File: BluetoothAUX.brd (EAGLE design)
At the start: 19.7 x 27.9 mm, 15 parts, among them IC2 TPA6132A2, J3 AUDIO_JACK_TRRSSMD_RA, J4 USB

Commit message: Make smaller
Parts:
- removed JP10: PROG, pinhead:1X08
- added JP1: PROG, pinhead:1X07
- moved R2 17.3 mm to (91.1, 24.4), turned to 90 degrees
- moved RN1 17.2 mm to (86.8, 24.4)
- moved R3 7.63 mm to (89.2, 24.4)
- moved LED1 4.44 mm to (79.4, 24.4)
- moved RN2 4.29 mm to (84.0, 24.4)
- moved IC2 3.52 mm to (79.7, 33.2)
- moved J3 3.49 mm to (87.6, 45.7)
- moved J4 3.35 mm to (78.7, 44.3)
- moved C5 3.33 mm to (81.6, 38.9)
- moved C4 2.13 mm to (85.7, 27.9), turned to 0 degrees
- moved C1 1.94 mm to (78.1, 36.7)
- moved C2 1.14 mm to (81.9, 27.9), turned to 0 degrees
- moved C3 1.14 mm to (78.1, 27.9), turned to 180 degrees
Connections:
- net USB_N renamed USBN
- net USB_P renamed USBP
- net +5V: no longer JP10.1
- net CLK: now also JP1.5; no longer JP10.6
- net CS: now also JP1.6; no longer JP10.7
- net G0: now also RN1.3; no longer RN1.2
- net G1: now also RN1.2; no longer RN1.1
- net GND: now also IC2.TH, JP1.1; no longer JP10.2
- net MISO: now also JP1.7; no longer JP10.8
- net MOSI: now also JP1.4; no longer JP10.5
- net RX: now also JP1.2; no longer JP10.3
- net TPA_EN: now also RN1.1; no longer RN1.3
- net TX: now also JP1.3; no longer JP10.4
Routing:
- net G1: track 7.53 -> 31.0 mm
- net POWER_EN: track 5.00 -> 20.9 mm
- net GND: track 4.30 -> 16.8 mm, vias 18 -> 32
- net +5V: track 36.0 -> 28.7 mm, vias 3 -> 2
- net USBP: track 19.5 -> 13.2 mm
- net G0: track 15.9 -> 21.6 mm, vias 2 -> 0
- net USBN: track 16.1 -> 10.9 mm
- net HVPDD: track 4.09 -> 6.71 mm
- net SPK_RN: track 11.4 -> 12.9 mm
- net TPA_EN: track 15.7 -> 14.5 mm
- net OUTL: track 13.3 -> 12.4 mm
- net SGND: track 12.2 -> 11.4 mm, vias 2 -> 0
- net SPK_LN: track 12.1 -> 12.8 mm
- net SPK_LP: track 15.0 -> 15.5 mm
- net OUTR: track 11.9 -> 12.5 mm
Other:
- board size 19.7 x 27.9 mm -> 19.7 x 24.4 mm

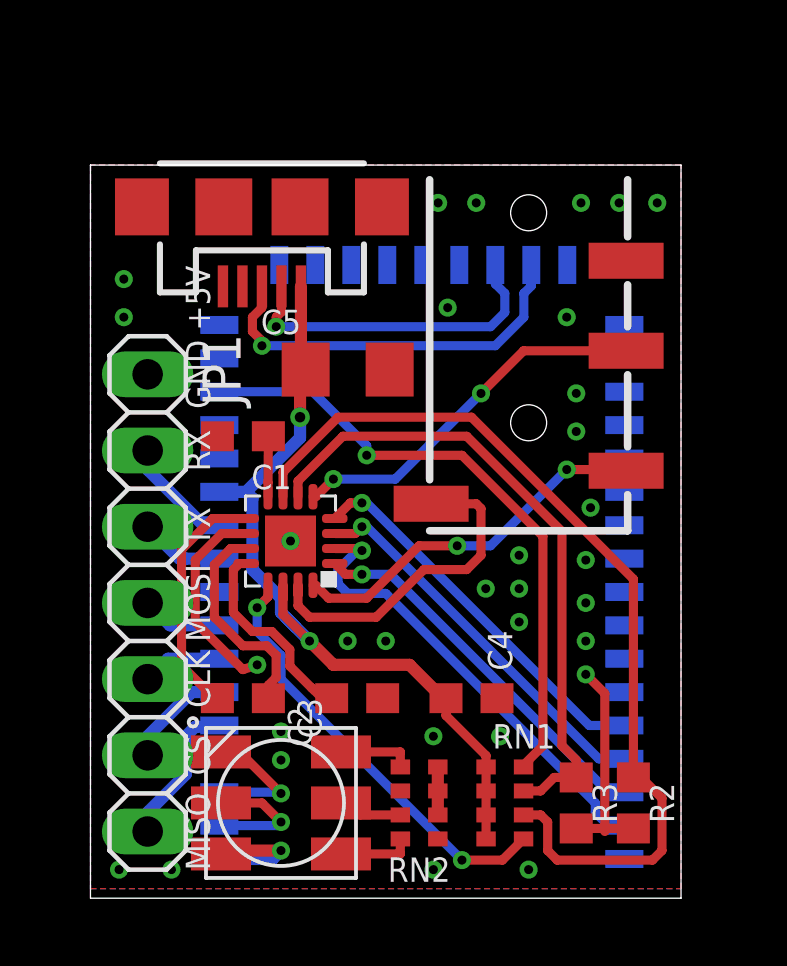
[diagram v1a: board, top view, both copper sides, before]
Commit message: VBAT_SENSE, POWER_EN, LEDs
Connect VBAT_SENSE to BAT
Delay on POWER_EN
Swap LED colors
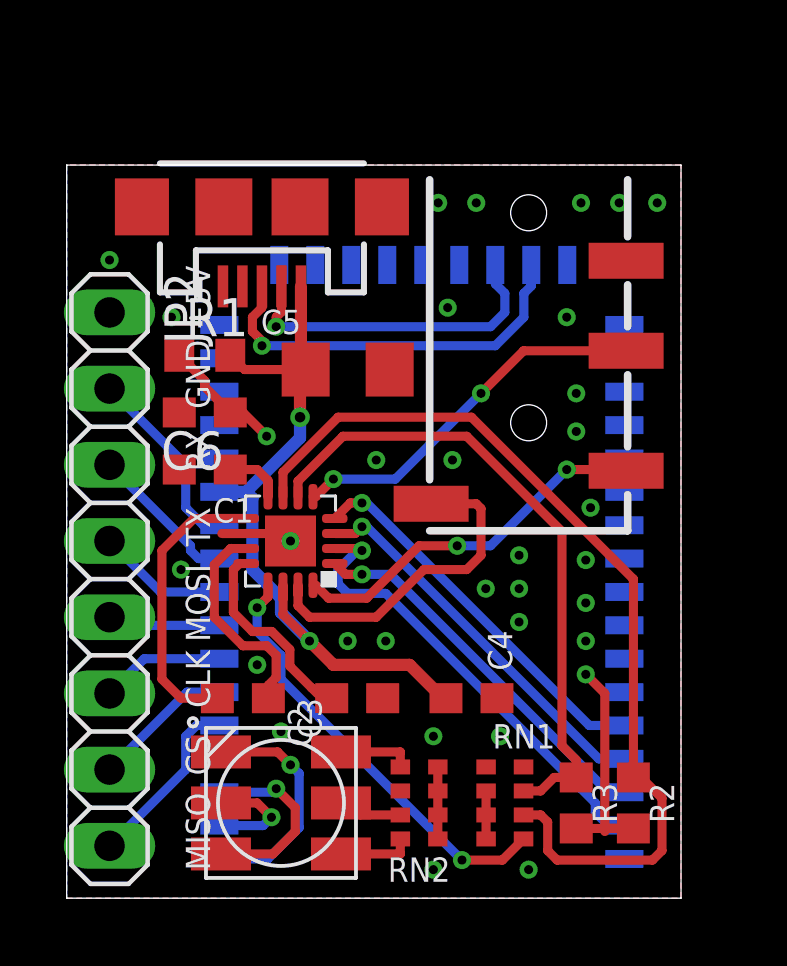
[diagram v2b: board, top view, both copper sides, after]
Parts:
- removed JP1: PROG, pinhead:1X07
- added C6: 470nF, resistor:C0603
- added JP2: (no value), pinhead:1X08
- added R1: 100K, resistor:R0603
- moved C1 1.69 mm to (76.8, 35.6)
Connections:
- net LED1 renamed N$3
- removed net BAT: U$1.P$14
- removed net LED0: LED1.4, U$1.P$3
- removed net LED2: LED1.6, U$1.P$1
- new net N$1: JP2.4, U$1.P$9
- new net N$2: LED1.6, U$1.P$3
- new net N$4: LED1.4, U$1.P$1
- new net N$5: U$1.P$14, U$1.P$19
- net +5V: now also R1.2, RN2.1, RN2.2, RN2.3, RN2.4; no longer RN1.5
- net CLK: now also JP2.6; no longer JP1.5
- net CS: now also JP2.7; no longer JP1.6
- net GND: now also C6.2, JP2.1; no longer JP1.1, RN2.1, RN2.2, RN2.3, RN2.4
- net MISO: now also JP2.8; no longer JP1.7
- net MOSI: now also JP2.5; no longer JP1.4
- net POWER_EN: now also C6.1, R1.1; no longer RN1.4
- net RX: now also JP2.2; no longer JP1.2
- net TX: now also JP2.3; no longer JP1.3
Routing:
- net POWER_EN: track 20.9 -> 6.45 mm
- net N$4: track 0.00 -> 7.80 mm, vias 0 -> 1
- net N$2: track 0.00 -> 6.66 mm, vias 0 -> 1
- net GND: track 16.8 -> 10.8 mm
- net LED0: track 4.88 -> 0.00 mm, vias 1 -> 0
- net N$1: track 0.00 -> 4.36 mm
- net LED2: track 4.18 -> 0.00 mm, vias 1 -> 0
- net CPN: track 8.09 -> 11.2 mm
- net RX: track 3.79 -> 6.38 mm
- net TX: track 3.04 -> 5.05 mm
- net CLK: track 2.67 -> 4.14 mm
- net CS: track 3.63 -> 4.73 mm
- net MOSI: track 2.70 -> 3.77 mm
- net MISO: track 4.97 -> 6.03 mm
- net +5V: track 28.7 -> 29.7 mm
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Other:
- board size 19.7 x 24.4 mm -> 20.5 x 24.4 mm

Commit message: Route
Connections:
- net N$5 renamed VBAT_SENSE
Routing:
- net VBAT_SENSE: track 0.00 -> 12.2 mm
- net +5V: track 29.7 -> 35.5 mm
- net GND: vias 32 -> 34
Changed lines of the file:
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@@
 <via x="91.91625" y="44.45" extent="1-16" drill="0.3"/>
 <contactref element="R3" pad="1"/>
-<via x="84.93125" y="40.9575" extent="1-16" drill="0.3"/>
+<via x="84.455" y="41.11625" extent="1-16" drill="0.3"/>
 <polygon width="0.3048" layer="16" isolate="0.254">
 <vertex x="92.71" y="45.72"/>
@@
 <via x="89.535" y="29.845" extent="1-16" drill="0.3"/>
 <via x="87.3125" y="32.7025" extent="1-16" drill="0.3"/>
-<via x="75.72375" y="40.64" extent="1-16" drill="0.3"/>
-<via x="73.66" y="42.545" extent="1-16" drill="0.3"/>
+<via x="74.295" y="42.545" extent="1-16" drill="0.3"/>
+<via x="73.025" y="42.545" extent="1-16" drill="0.3"/>
 <via x="90.64625" y="44.45" extent="1-16" drill="0.3"/>
 <via x="78.58125" y="29.05125" extent="1-16" drill="0.3"/>
@@
 <via x="82.55" y="35.8775" extent="1-16" drill="0.3"/>
 <via x="85.09" y="35.8775" extent="1-16" drill="0.3"/>
+<via x="83.185" y="41.11625" extent="1-16" drill="0.3"/>
+<via x="85.725" y="41.11625" extent="1-16" drill="0.3"/>
 </signal>
 <signal name="+5V" class="1">
@@
 <contactref element="RN2" pad="3"/>
 <contactref element="RN2" pad="4"/>
-<wire x1="84.60375" y1="24.8475" x2="84.60375" y2="25.6475" width="0.3048" layer="1"/>
+<wire x1="84.60375" y1="25.6475" x2="84.60375" y2="24.8475" width="0.3048" layer="1"/>
 <wire x1="84.60375" y1="24.8475" x2="84.60375" y2="24.0475" width="0.3048" layer="1"/>
 <wire x1="84.60375" y1="24.0475" x2="84.60375" y2="23.2475" width="0.3048" layer="1"/>
@@
 <wire x1="77.685" y1="39.37" x2="78.16125" y2="38.89375" width="0.3048" layer="1"/>
 <wire x1="78.16125" y1="38.89375" x2="80.1975" y2="38.89375" width="0.3048" layer="1"/>
-<wire x1="84.60375" y1="24.8475" x2="86.21125" y2="24.8475" width="0" layer="19" extent="1-1"/>
-<wire x1="84.7725" y1="27.94" x2="84.60375" y2="25.6475" width="0" layer="19" extent="1-1"/>
+<wire x1="84.7725" y1="27.94" x2="85.4075" y2="27.305" width="0.3048" layer="1"/>
+<wire x1="84.60375" y1="24.8475" x2="86.21125" y2="24.8475" width="0.3048" layer="1"/>
+<wire x1="85.4075" y1="24.8475" x2="86.21125" y2="24.8475" width="0.3048" layer="1"/>
+<wire x1="85.4075" y1="27.305" x2="85.4075" y2="24.8475" width="0.3048" layer="1"/>
 </signal>
 <signal name="VBUS_1.8V">
@@
 <wire x1="78.89875" y1="36.67125" x2="78.105" y2="37.465" width="0.3048" layer="1"/>
 <wire x1="78.105" y1="37.465" x2="77.685" y2="37.465" width="0.3048" layer="1"/>
-<wire x1="77.415" y1="38.155" x2="78.89875" y2="36.67125" width="0.3048" layer="16"/>
 <wire x1="76.835" y1="38.52" x2="75.985" y2="39.37" width="0.3048" layer="1"/>
 <wire x1="76.835" y1="38.52" x2="76.835" y2="38.4175" width="0.3048" layer="1"/>
 <wire x1="77.685" y1="37.465" x2="76.835" y2="38.315" width="0.3048" layer="1"/>
-<wire x1="76.835" y1="38.315" x2="76.835" y2="38.52" width="0.3048" layer="1"/>
+<wire x1="76.835" y1="38.315" x2="76.835" y2="38.4175" width="0.3048" layer="1"/>
+<wire x1="77.415" y1="38.155" x2="77.47" y2="38.1" width="0.3048" layer="16"/>
+<wire x1="77.47" y1="38.1" x2="78.105" y2="38.1" width="0.3048" layer="16"/>
+<wire x1="78.105" y1="38.1" x2="78.89875" y2="37.30625" width="0.3048" layer="16"/>
+<wire x1="78.89875" y1="37.30625" x2="78.89875" y2="36.67125" width="0.3048" layer="16"/>
 </signal>
 <signal name="USBN">
@@
 <wire x1="79.9822" y1="23.62595" x2="79.9822" y2="25.4278" width="0.3048" layer="16"/>
 </signal>
-<signal name="N$5">
+<signal name="VBAT_SENSE">
 <contactref element="U$1" pad="P$19"/>
 <contactref element="U$1" pad="P$14"/>
-<wire x1="77.32" y1="37.0425" x2="80.52" y2="42.38" width="0" layer="19" extent="16-16"/>
+<wire x1="80.52" y1="42.38" x2="80.52" y2="43.14625" width="0.3048" layer="16"/>
+<wire x1="80.52" y1="43.14625" x2="80.01" y2="43.65625" width="0.3048" layer="16"/>
+<wire x1="80.01" y1="43.65625" x2="77.94625" y2="43.65625" width="0.3048" layer="16"/>
+<wire x1="77.94625" y1="43.65625" x2="75.8825" y2="41.5925" width="0.3048" layer="16"/>
+<wire x1="75.8825" y1="37.465" x2="75.8825" y2="41.5925" width="0.3048" layer="16"/>
+<wire x1="77.32" y1="37.0425" x2="76.305" y2="37.0425" width="0.3048" layer="16"/>
+<wire x1="76.305" y1="37.0425" x2="75.8825" y2="37.465" width="0.3048" layer="16"/>
 </signal>
 </signals>

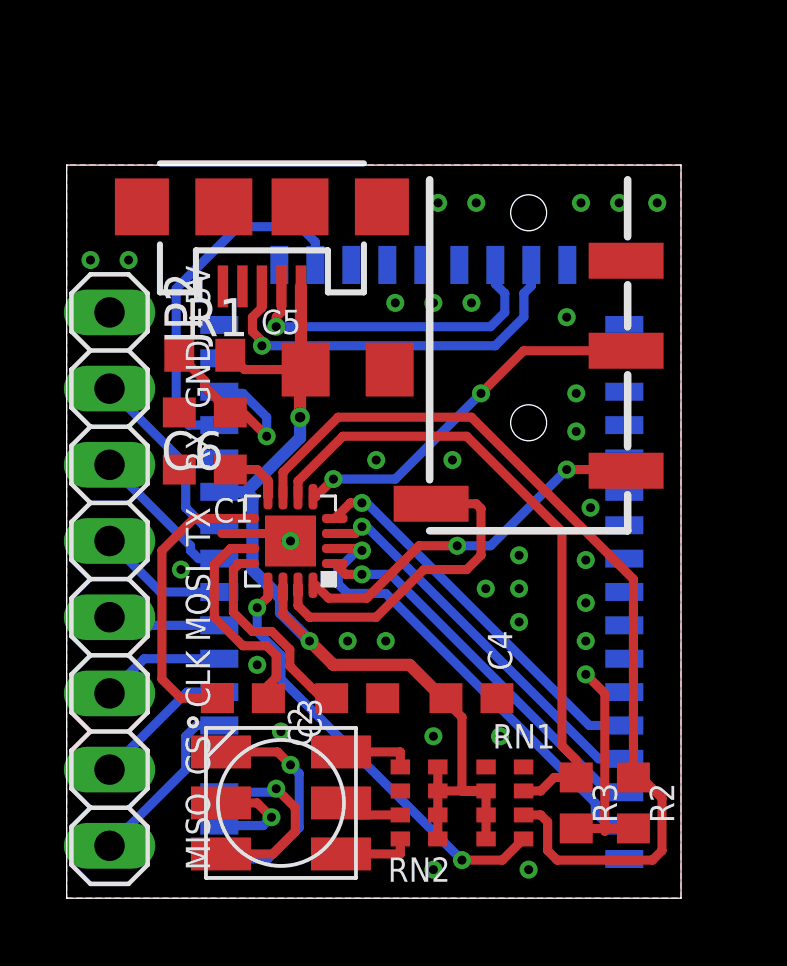
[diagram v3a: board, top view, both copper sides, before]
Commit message: Delay circuit with MOSFET
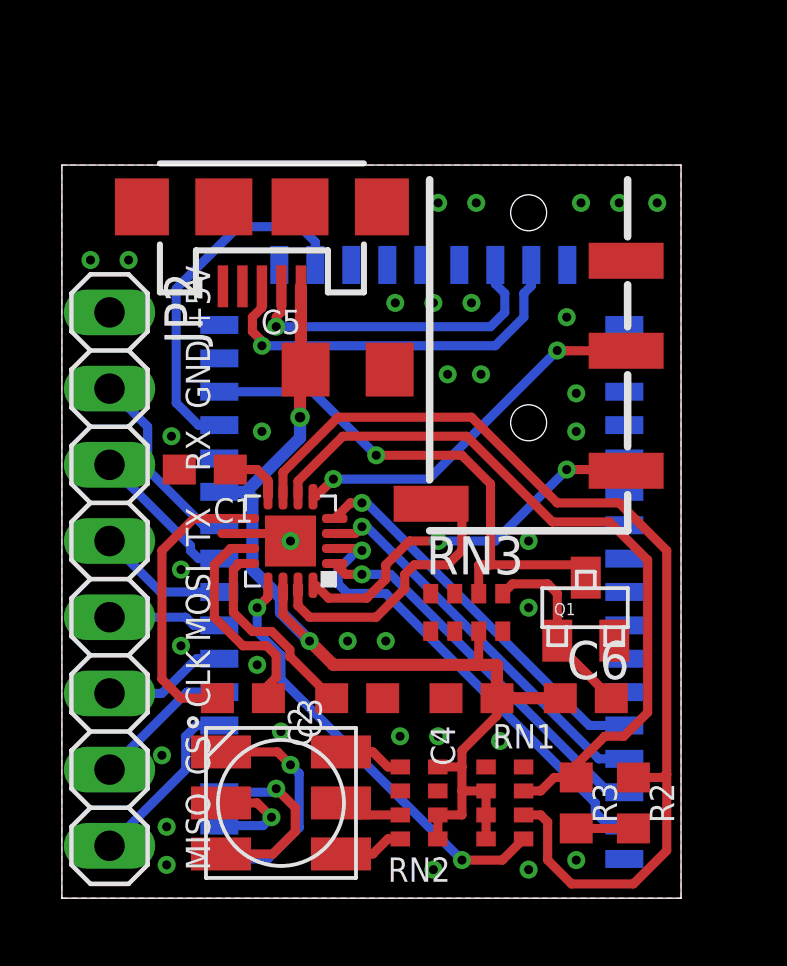
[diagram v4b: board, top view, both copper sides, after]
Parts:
- removed R1: 100K, resistor:R0603
- added Q1: FDV301N, FDV301N:SOT-23
- added RN3: 100K, resistor-dil:0603-ARC
- moved C6 15.9 mm to (89.5, 27.9), turned to 0 degrees
- turned C4 to 180 degrees
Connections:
- new net N$5: C6.2, Q1.P$1, RN3.1
- net +5V: now also C6.1, RN3.7; no longer R1.2, RN2.3
- net GND: now also Q1.P$2, RN3.8; no longer C6.2
- net POWER_EN: now also Q1.P$3, RN3.2; no longer C6.1, R1.1
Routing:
- net POWER_EN: track 6.72 -> 17.9 mm
- net N$5: track 0.00 -> 6.93 mm
- net GND: track 10.8 -> 4.30 mm, vias 34 -> 35
- net G1: track 31.0 -> 34.5 mm
- net G0: track 21.6 -> 25.1 mm
- net +5V: track 35.5 -> 38.5 mm
- net SGND: track 11.4 -> 10.4 mm
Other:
- board size 20.5 x 24.4 mm -> 20.6 x 24.4 mm

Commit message: SPI_PCM resistor
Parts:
- added R1: 0, resistor:R0603
- moved C1 2.38 mm to (76.8, 37.9)
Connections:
- new net SPI_PCM: JP2.4, R1.1
- net +5V: now also RN1.5, RN2.3
- net N$1: now also R1.2; no longer JP2.4
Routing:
- net SPI_PCM: track 0.00 -> 4.06 mm
- net GND: track 4.30 -> 8.12 mm
- net N$1: track 4.36 -> 7.11 mm, vias 0 -> 1
- net +5V: track 38.5 -> 41.2 mm
- net HPVSS: track 2.43 -> 4.81 mm
- net CPN: track 11.2 -> 10.0 mm

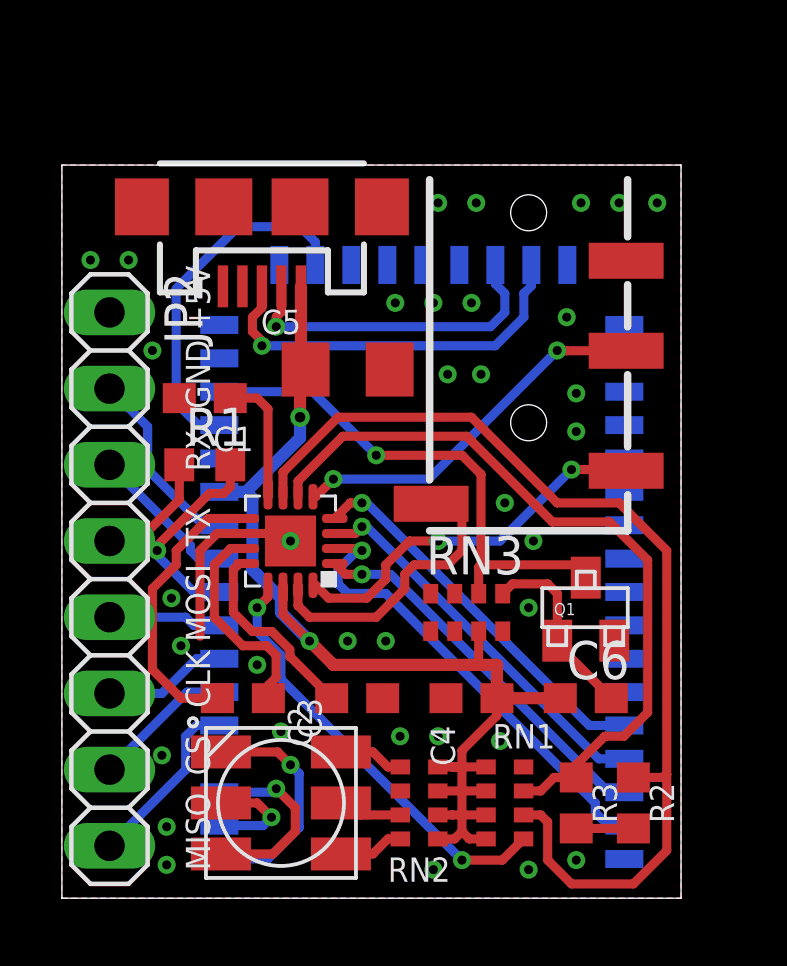
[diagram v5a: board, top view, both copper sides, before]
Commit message: DIP switch, 4-pin LED, Powerup fix
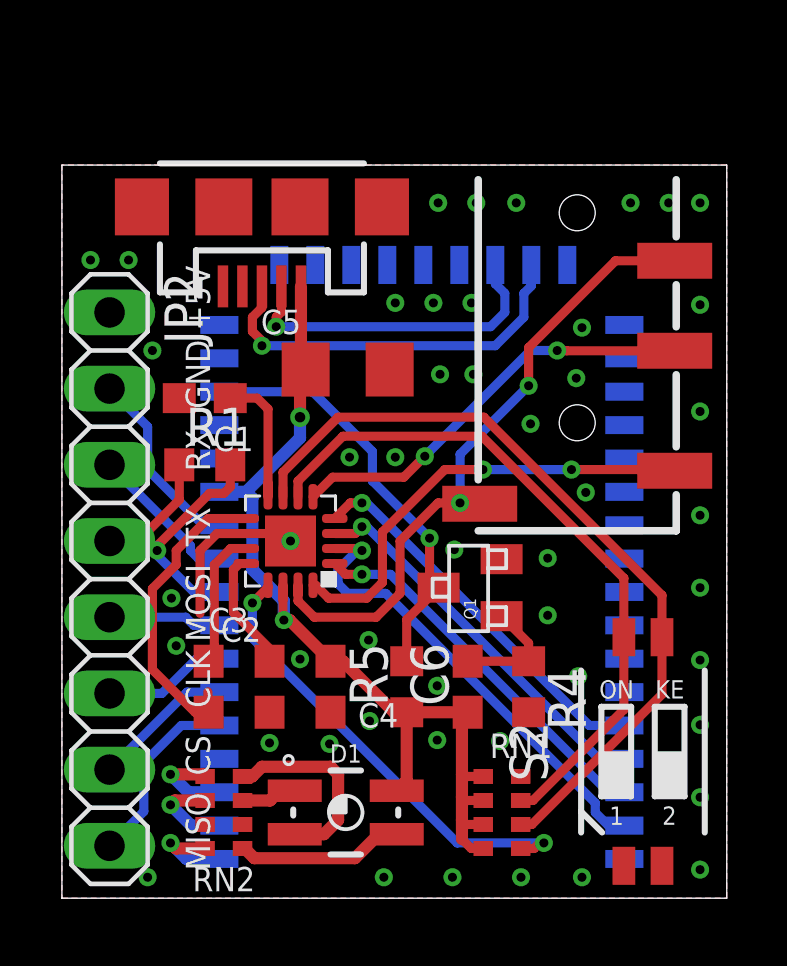
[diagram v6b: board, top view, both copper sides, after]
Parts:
- removed LED1: RGBLED5050, adafruit:RGBLED5050
- removed R2, R3: 0, resistor:R0603
- removed RN3: 100K, resistor-dil:0603-ARC
- added D1: RGB, SparkFun-LED:P-LCC-4-3
- added R4: 400K, resistor:R0603
- added R5: 100K, resistor:R0603
- added S2: DSHP02TSGER, BluetoothAUX:DSHP02TSGER
- C6: value 470nF -> 2.2uF
- R1: value 0 -> 10K
- RN2: value 220 -> 470
- moved RN2 6.52 mm to (77.5, 24.1)
- moved C4 4.71 mm to (81.0, 28.3), turned to 270 degrees
- moved Q1 3.96 mm to (85.6, 31.6), turned to 90 degrees
- moved C6 3.96 mm to (85.6, 28.3), turned to 90 degrees
- moved C2 2.95 mm to (79.0, 28.3), turned to 270 degrees
- moved J3 1.62 mm to (89.2, 45.7)
- moved C3 1.20 mm to (77.0, 28.3), turned to 270 degrees
- moved RN1 0.33 mm to (86.7, 24.1)
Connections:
- removed net LED_B: LED1.3, RN2.5
- removed net LED_G: LED1.1, RN2.8
- removed net LED_R: LED1.2, RN2.7
- removed net VBAT_SENSE: U$1.P$14, U$1.P$19
- new net BAT: U$1.P$14
- new net BLUE: RN2.8, U$1.P$1
- new net GREEN: RN2.5, U$1.P$3
- new net RED: RN2.6, U$1.P$2
- net +5V: now also D1.4, R5.1; no longer RN2.1, RN2.2, RN2.3, RN2.4, RN3.7
- net G0: now also S2.4; no longer R3.2
- net G1: now also S2.3; no longer R2.2
- net GND: now also R4.2, S2.1, S2.2; no longer R2.1, R3.1, RN3.8
- net N$2: now also D1.2, RN2.4; no longer LED1.6, U$1.P$3
- net N$3: now also D1.1, RN2.3; no longer LED1.5, U$1.P$2
- net N$4: now also D1.3, RN2.1; no longer LED1.4, U$1.P$1
- net N$5: now also R4.1; no longer RN3.1
- net POWER_EN: now also R5.2; no longer RN3.2
- net SGND: now also J3.RING2
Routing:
- net VBAT_SENSE: track 12.0 -> 0.00 mm
- net SGND: track 10.4 -> 22.1 mm, vias 0 -> 2
- net G1: track 34.5 -> 26.5 mm
- net +5V: track 41.2 -> 34.1 mm
- net RED: track 0.00 -> 3.13 mm, vias 0 -> 1
- net POWER_EN: track 17.7 -> 14.6 mm
- net BLUE: track 0.00 -> 3.08 mm, vias 0 -> 1
- net GREEN: track 0.00 -> 3.06 mm, vias 0 -> 1
- net N$5: track 6.93 -> 3.91 mm
- net GND: track 8.12 -> 5.45 mm, vias 35 -> 48
- net CPP: track 7.16 -> 4.54 mm
- net HVPDD: track 6.54 -> 4.09 mm
- net OUTL: track 12.7 -> 15.0 mm
- net N$4: track 7.80 -> 5.60 mm, vias 1 -> 0
- net LED_G: track 2.19 -> 0.00 mm
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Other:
- board size 20.6 x 24.4 mm -> 22.2 x 24.4 mm
